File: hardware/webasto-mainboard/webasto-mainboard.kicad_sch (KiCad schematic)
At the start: 7 parts, among them J1 Console FTDI, J2 DEBUG, Q1 DMG2301L, U1 Pico, U2 LM4040DBZ-2.0

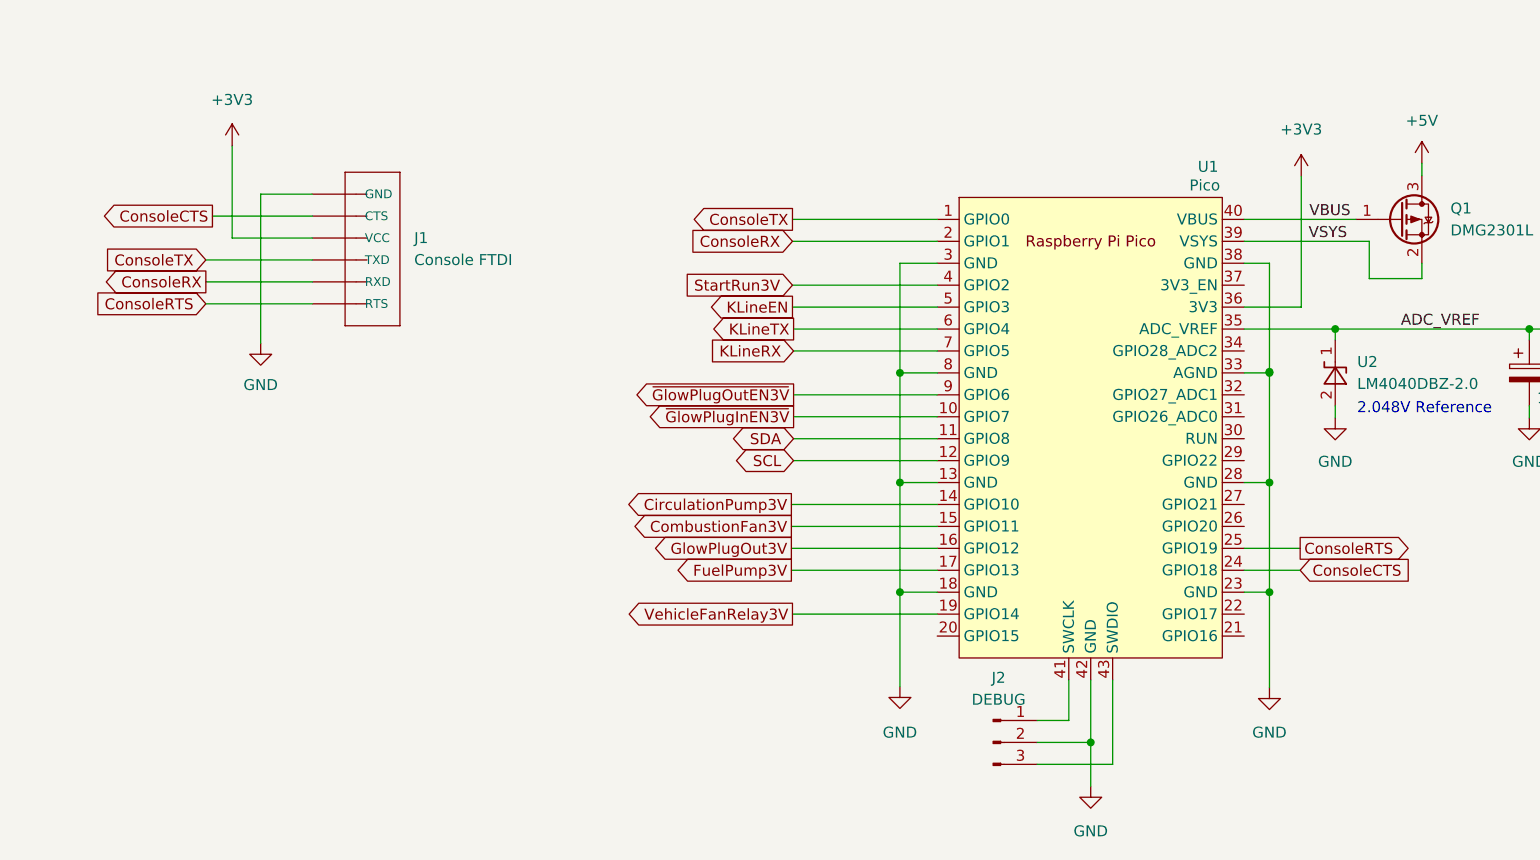
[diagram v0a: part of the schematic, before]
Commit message: Added a 4kbit FRAM on the mainboard to hold nonvolatile
- things like burn hours.
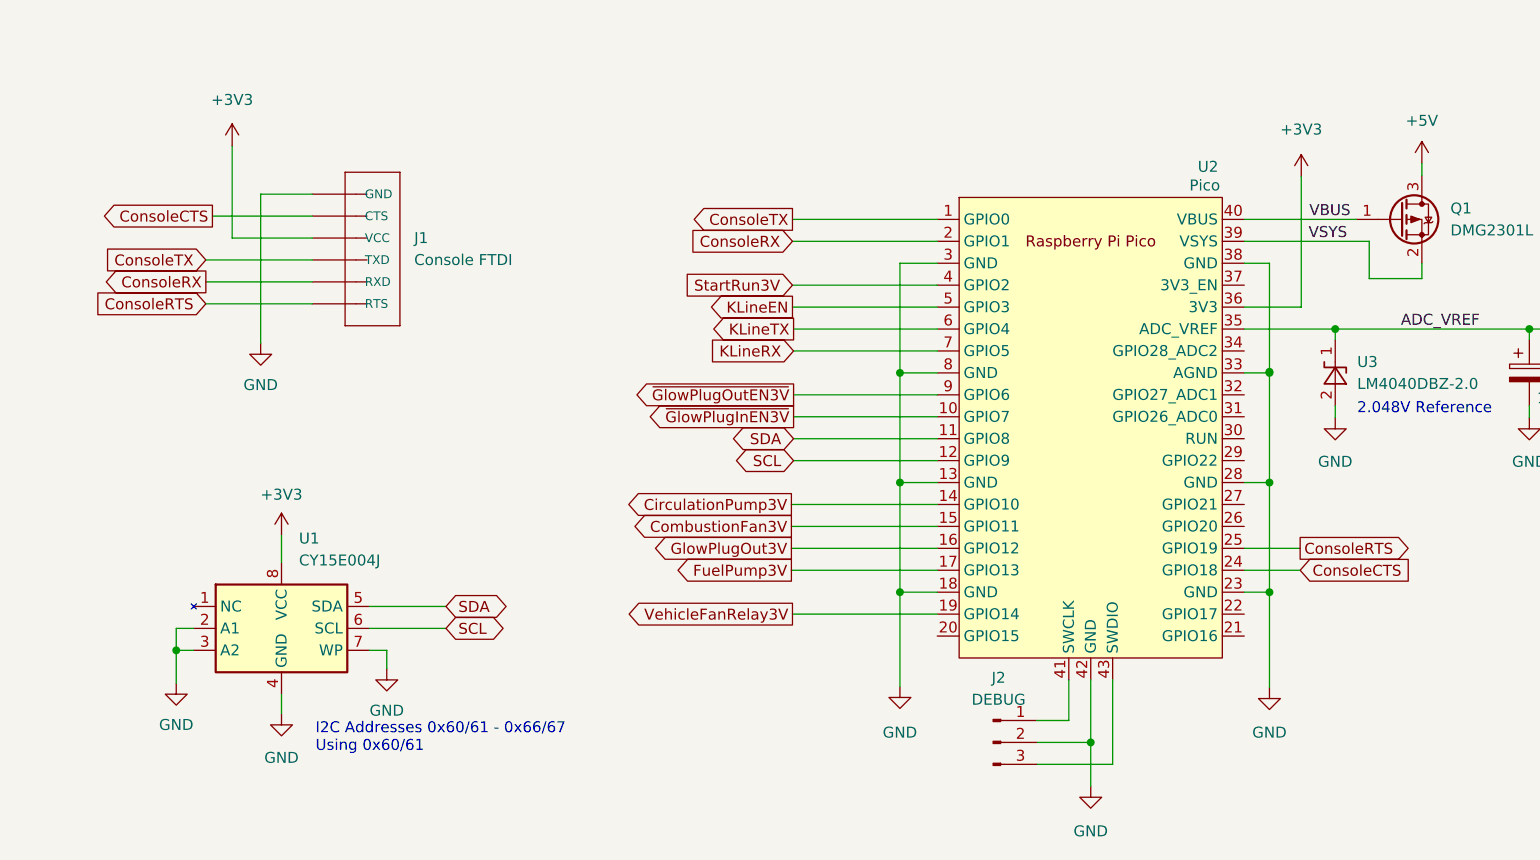
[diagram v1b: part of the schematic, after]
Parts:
- added U1: CY15E004J, Package_SO:SOIC-8_5.23x5.23mm_P1.27mm, symbol Beirdo:CY15E004J
- J1: footprint FTDI_BASIC -> Beirdo:FTDI_BASIC
- renumbered U1 to U2, U2 to U3
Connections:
- net +3V3: now also U1.8 (VCC)
- net GND: now also U1.2 (A1), U1.3 (A2), U1.4 (GND), U1.7 (WP)
- net SCL: now also U1.6 (SCL)
- net SDA: now also U1.5 (SDA)
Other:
- note added: "I2C Addresses 0x60/61 - 0x66/67 Using 0x60/61"

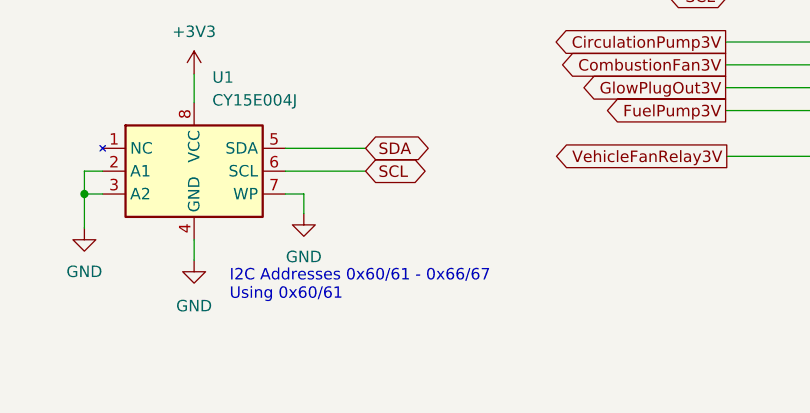
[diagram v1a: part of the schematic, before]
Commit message: Add support for the NVM variables in the FRAM
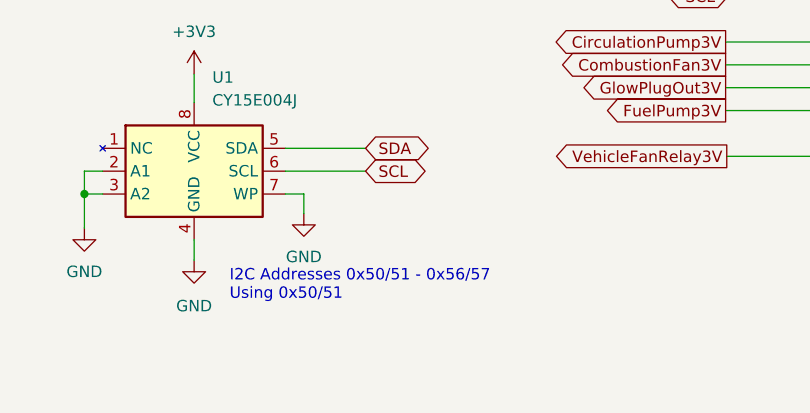
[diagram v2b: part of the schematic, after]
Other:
- note added: "I2C Addresses 0x50/51 - 0x56/57 Using 0x50/51"
- note removed: "I2C Addresses 0x60/61 - 0x66/67 Using 0x60/61"
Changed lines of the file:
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@@
     (stroke (width 0) (type default) (color 0 0 0 0))
   )
-  (text "I2C Addresses 0x60/61 - 0x66/67\nUsing 0x60/61" (at 54.61 158.242 0)
+  (text "I2C Addresses 0x50/51 - 0x56/57\nUsing 0x50/51" (at 54.61 158.242 0)
     (effects (font (size 1.27 1.27)) (justify left bottom))
   )

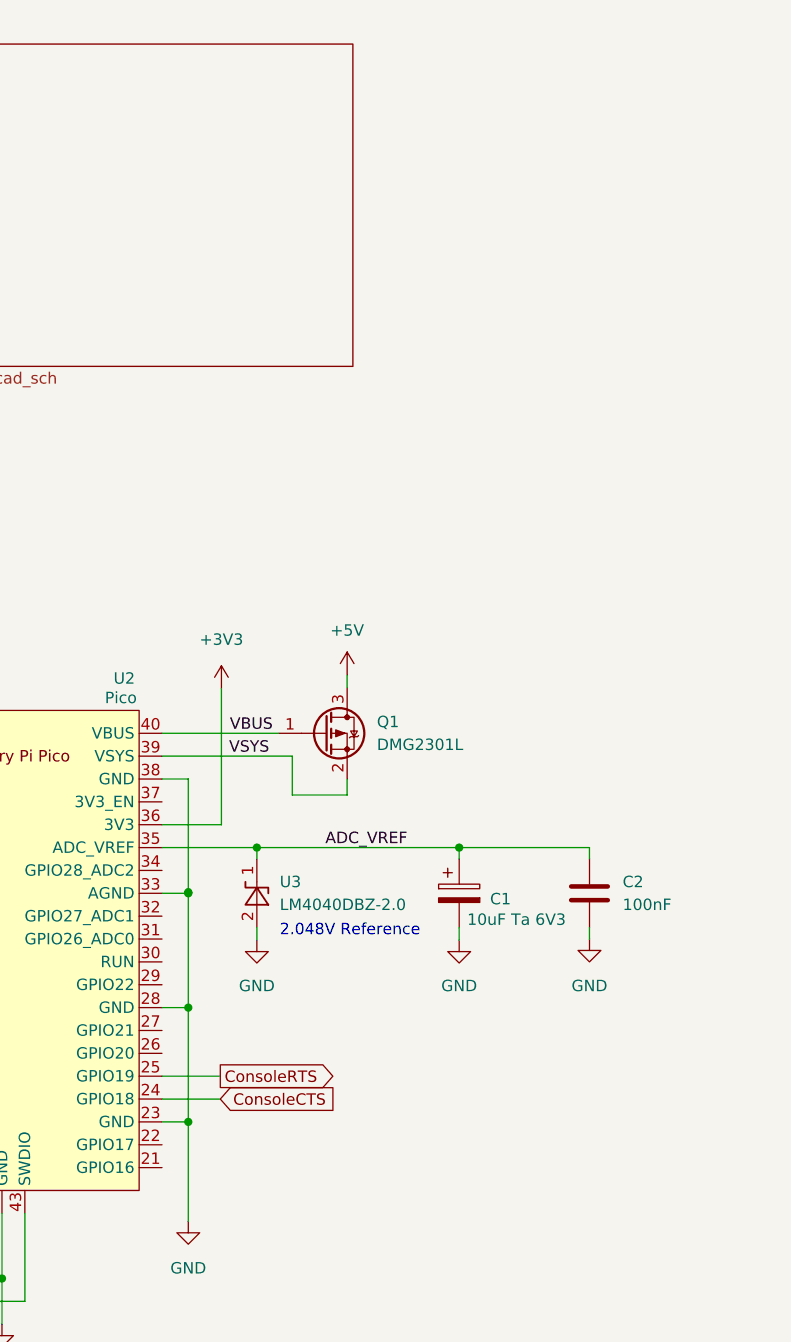
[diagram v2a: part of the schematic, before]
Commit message: Added EmergencyStop input.  Hope I never need it.
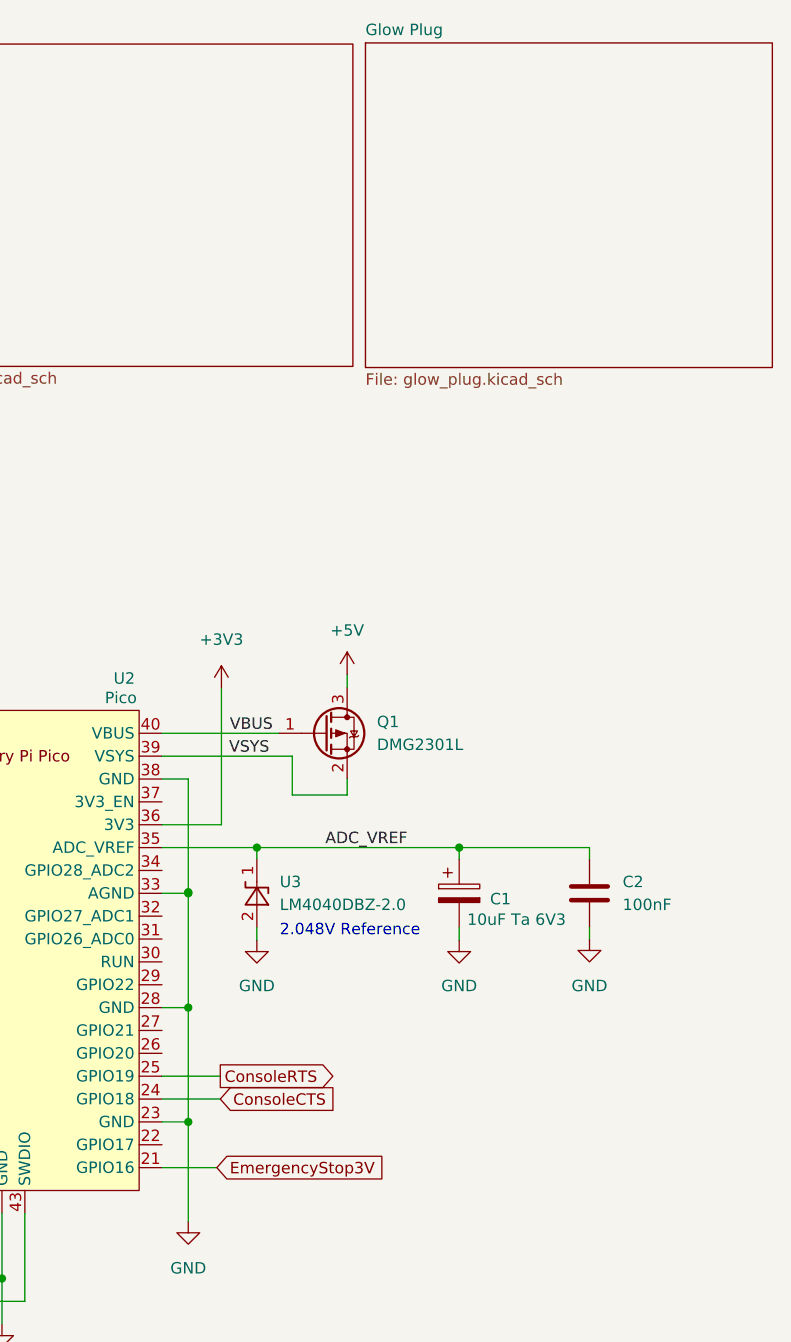
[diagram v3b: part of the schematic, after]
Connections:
- net EmergencyStop3V: now reaches U2.21 (GPIO16)
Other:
- added sheet Glow Plug (glow_plug.kicad_sch)

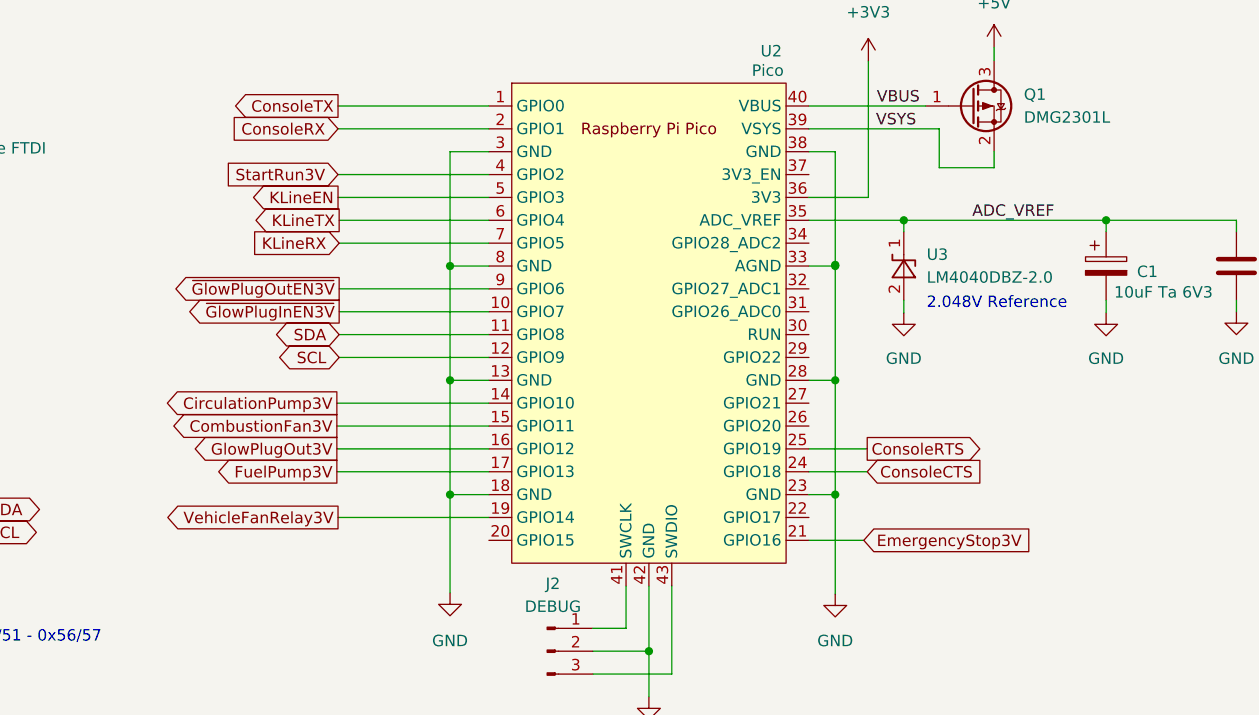
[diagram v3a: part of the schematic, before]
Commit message: Oops.  StartRun is active at +12V.  Change the level translation.
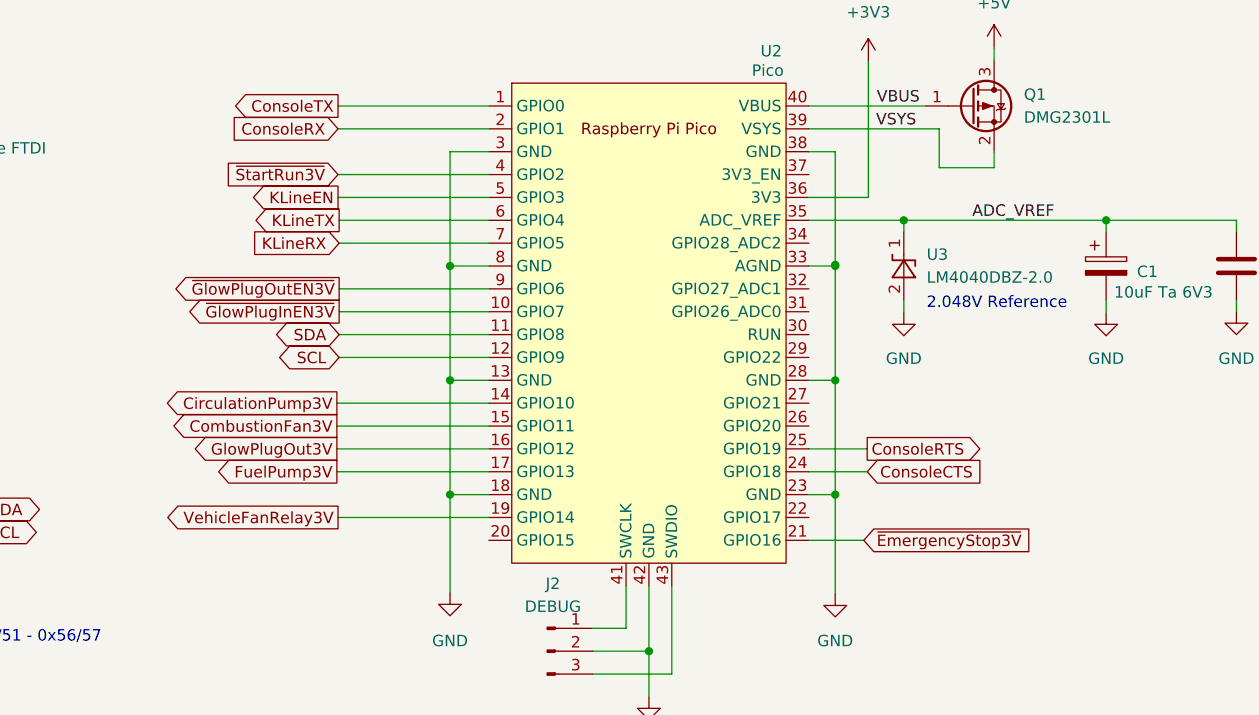
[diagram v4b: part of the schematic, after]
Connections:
- net EmergencyStop3V renamed ~{EmergencyStop3V}
- net StartRun3V renamed ~{StartRun3V}

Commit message: Oops, forgot to check in the schematic
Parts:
- added D? (x2): LED, symbol Device:LED
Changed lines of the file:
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@@
+    )
+  )
+  (global_label "~{OperatingLED}" (shape input) (at 236.728 84.836 180) (fields_autoplaced)
+    (effects (font (size 1.27 1.27)) (justify right))
+    (property "Intersheet References" "${INTERSHEET_REFS}" (id 0) (at 221.7359 84.7566 0)
+      (effects (font (size 1.27 1.27)) (justify right) hide)
     )
   )
@@
     (effects (font (size 1.27 1.27)) (justify right))
     (property "Intersheet References" "${INTERSHEET_REFS}" (id 0) (at 29.5183 103.5526 0)
+      (effects (font (size 1.27 1.27)) (justify right) hide)
+    )
+  )
+  (global_label "~{FlameLED}" (shape input) (at 236.347 91.313 180) (fields_autoplaced)
+    (effects (font (size 1.27 1.27)) (justify right))
+    (property "Intersheet References" "${INTERSHEET_REFS}" (id 0) (at 224.802 91.2336 0)
       (effects (font (size 1.27 1.27)) (justify right) hide)
     )
@@
     (pin "8")
   )
+  (symbol (lib_id "Device:LED") (at 246.253 97.155 90) (unit 1)
+    (in_bom yes) (on_board yes) (fields_autoplaced)
+    (property "Reference" "D?" (id 0) (at 250.19 97.4724 90)
+      (effects (font (size 1.27 1.27)) (justify right))
+    )
+    (property "Value" "LED" (id 1) (at 250.19 100.0124 90)
+      (effects (font (size 1.27 1.27)) (justify right))
+    )
+    (property "Footprint" "" (id 2) (at 246.253 97.155 0)
+      (effects (font (size 1.27 1.27)) hide)
+    )
+    (property "Datasheet" "~" (id 3) (at 246.253 97.155 0)
+      (effects (font (size 1.27 1.27)) hide)
+    )
+    (pin "1")
+    (pin "2")
+  )
   (symbol (lib_id "power:GND") (at 38.481 150.114 0) (unit 1)
     (in_bom yes) (on_board yes) (fields_autoplaced)
@@
     )
     (pin "1")
+  )
+  (symbol (lib_id "Device:LED") (at 261.747 98.044 90) (unit 1)
+    (in_bom yes) (on_board yes) (fields_autoplaced)
+    (property "Reference" "D?" (id 0) (at 265.43 98.3614 90)
+      (effects (font (size 1.27 1.27)) (justify right))
+    )
+    (property "Value" "LED" (id 1) (at 265.43 100.9014 90)
+      (effects (font (size 1.27 1.27)) (justify right))
+    )
+    (property "Footprint" "" (id 2) (at 261.747 98.044 0)
+      (effects (font (size 1.27 1.27)) hide)
+    )
+    (property "Datasheet" "~" (id 3) (at 261.747 98.044 0)
+      (effects (font (size 1.27 1.27)) hide)
+    )
+    (pin "1")
+    (pin "2")
   )
   (symbol (lib_name "+3V3_1") (lib_id "power:+3V3") (at 44.958 87.884 0) (unit 1)
@@
       (reference "D5") (unit 1) (value "ACDBQC0130L-HF") (footprint "Diode_SMD:D_SOD-923")
     )
+    (path "/d881c022-c797-47e8-af8c-bad1e357032b"
+      (reference "D?") (unit 1) (value "LED") (footprint "")
+    )
+    (path "/ed00d4cd-3d17-49f2-bd19-a7ddb695e0ee"
+      (reference "D?") (unit 1) (value "LED") (footprint "")
+    )
     (path "/7d073a75-c0a6-4467-8507-95514c8d14f0/27fdbf94-7bcf-49a5-a656-e11cf99c6a9b"
